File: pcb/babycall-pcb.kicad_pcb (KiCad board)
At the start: 2 copper layers, 1 part, among them U1 ESP32-C3-MINI-1-H4X

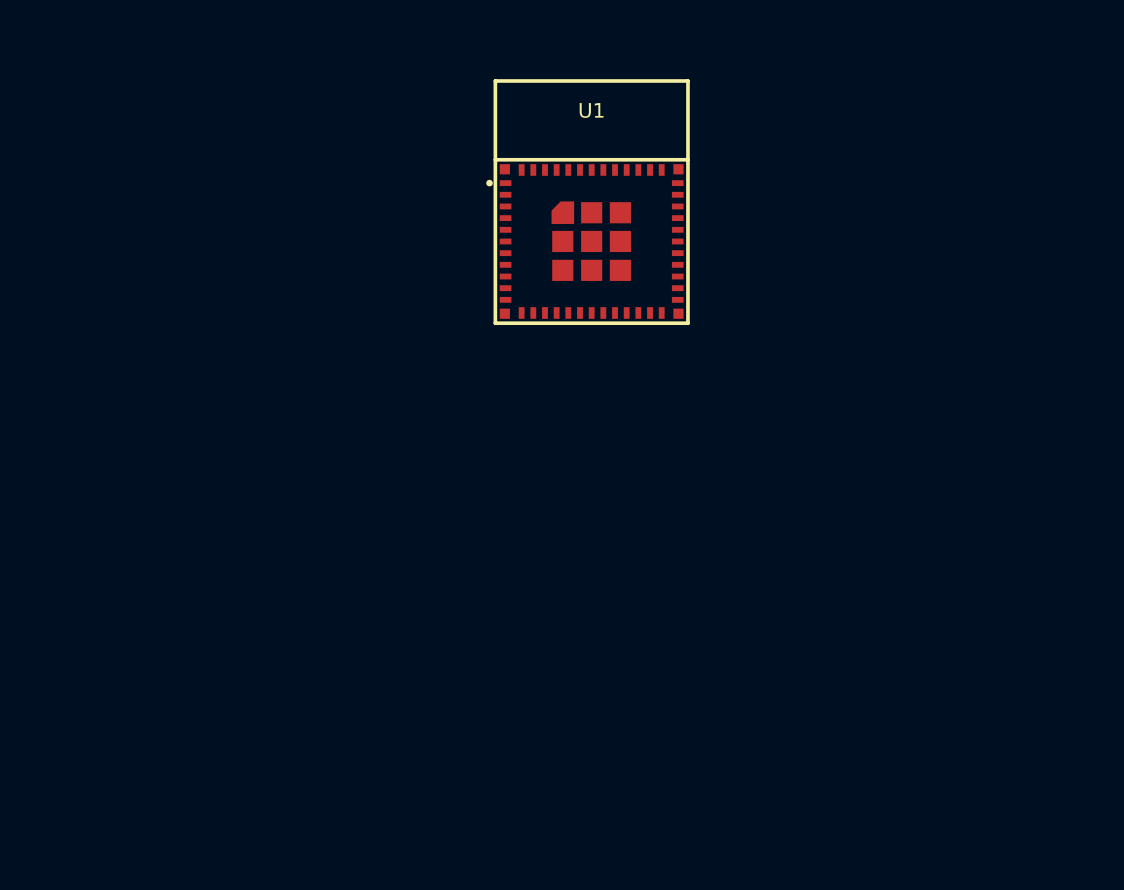
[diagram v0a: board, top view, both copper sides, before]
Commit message: Claude stuff, and gitignore
Also some models for pcb
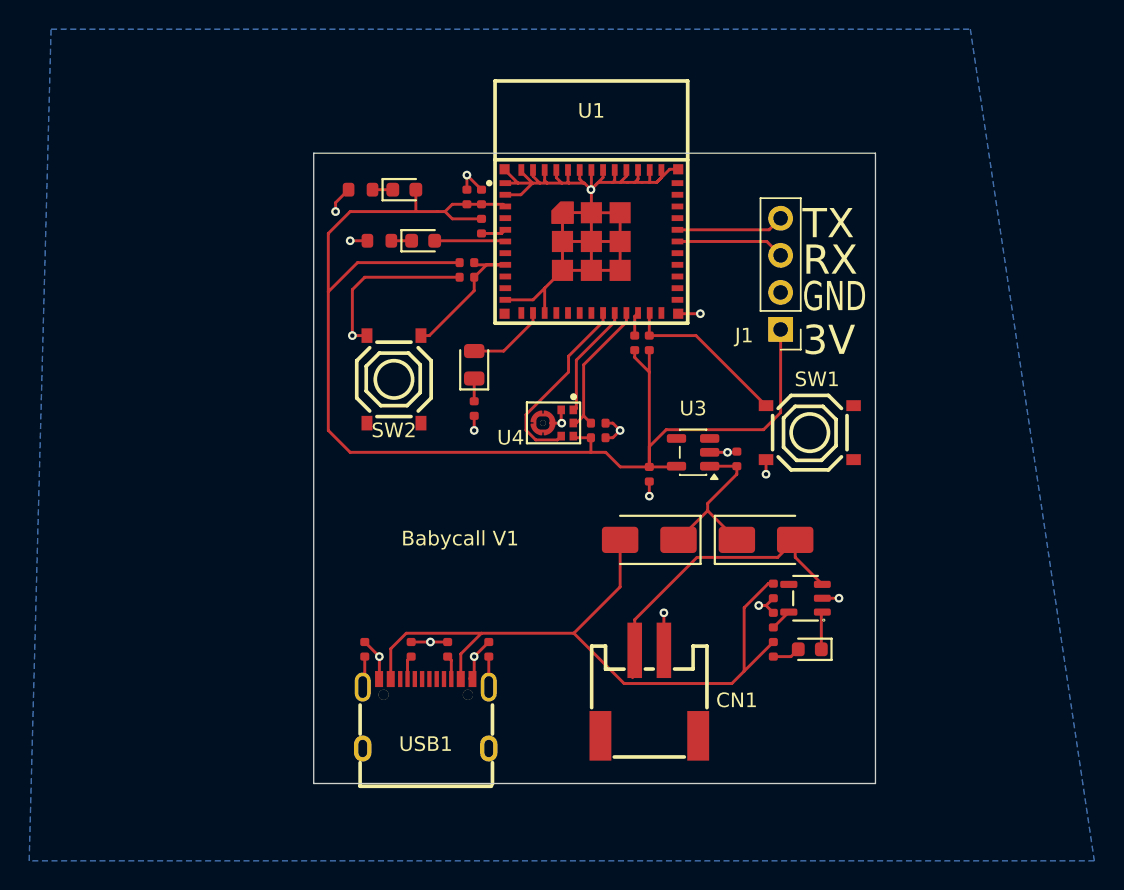
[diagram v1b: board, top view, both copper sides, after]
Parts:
- added C1: 1uF, PCM_JLCPCB:C_0402, F.Cu at (144.5, 90.0)
- added C10: 1uF, PCM_JLCPCB:C_0402, F.Cu at (162.0, 108.0)
- added C11: 1uF, PCM_JLCPCB:C_0402, F.Cu at (156.0, 109.0)
- added C12: 1uF, PCM_JLCPCB:C_0402, F.Cu at (152.5, 106.5)
- added C2: 100nF, PCM_JLCPCB:C_0402, F.Cu at (143.5, 90.0)
- added C3: 1uF, PCM_JLCPCB:C_0402, F.Cu at (143.5, 95.5)
- added C7: 100nF, PCM_JLCPCB:C_0402, F.Cu at (136.5, 121.0)
- added C8: 100nF, PCM_JLCPCB:C_0402, F.Cu at (145.0, 121.0)
- added C9: 1uF, PCM_JLCPCB:C_0402, F.Cu at (164.5, 117.0)
- added CN1: S2B-PH-SM4-TB(LF)(SN), jlcpcb:CONN-SMD_P2.00_S2B-PH-SM4-TB-LF-SN, F.Cu at (156.0, 124.0)
- added D2: Red, PCM_JLCPCB:D_0603, F.Cu at (139.2, 89.5)
- added D3: Green, PCM_JLCPCB:D_0805, F.Cu at (144.0, 101.5)
- added D4: Yellow, PCM_JLCPCB:D_0603, F.Cu at (140.5, 93.0)
- added D5: Red, PCM_JLCPCB:D_0603, F.Cu at (167.0, 121.0)
- added D6: SS34, PCM_JLCPCB:D_SMA, F.Cu at (156.0, 113.5)
- added D7: SS34, PCM_JLCPCB:D_SMA, F.Cu at (164.0, 113.5)
- added J1: Conn_01x04_Pin, Connector_PinHeader_2.54mm:PinHeader_1x04_P2.54mm_Vertical, F.Cu at (165.0, 99.1)
- added R1: 10kΩ, PCM_JLCPCB:R_0402, F.Cu at (143.5, 94.5)
- added R10: 270Ω, PCM_JLCPCB:R_0603, F.Cu at (136.2, 89.5)
- added R11: 220Ω, PCM_JLCPCB:R_0402, F.Cu at (144.0, 104.5)
- added R12: 270Ω, PCM_JLCPCB:R_0603, F.Cu at (137.5, 93.0)
- added R13: 100kΩ, PCM_JLCPCB:R_0402, F.Cu at (152.5, 105.5)
- added R14: 330Ω, PCM_JLCPCB:R_0402, F.Cu at (164.5, 121.0)
- added R2: 4.7kΩ, PCM_JLCPCB:R_0402, F.Cu at (164.5, 119.0)
- added R3: 10kΩ, PCM_JLCPCB:R_0402, F.Cu at (144.5, 92.0)
- added R4: 10kΩ, PCM_JLCPCB:R_0402, F.Cu at (155.0, 100.0)
- added R6: 10kΩ, PCM_JLCPCB:R_0402, F.Cu at (156.0, 100.0)
- added R7: 5.1kΩ, PCM_JLCPCB:R_0402, F.Cu at (142.2, 121.0)
- added R8: 5.1kΩ, PCM_JLCPCB:R_0402, F.Cu at (139.7, 121.0)
- added SW1: TS-1187A-B-A-B, jlcpcb:SW-SMD_4P-L5.1-W5.1-P3.70-LS6.5-TL_H1.5, F.Cu at (167.0, 106.2)
- added SW2: TS-1187A-B-A-B, jlcpcb:SW-SMD_4P-L5.1-W5.1-P3.70-LS6.5-TL_H1.5, F.Cu at (138.5, 102.5)
- added U3: AP2112K-3.3, Package_TO_SOT_SMD:SOT-23-5, F.Cu at (159.0, 107.5)
- added U4: ICS-43434_C5656610, jlcpcb:MIC-SMD_6P-L3.5-W2.7-P0.90-BL, F.Cu at (149.5, 105.5)
- added U5: TP4054, PCM_JLCPCB:SOT-23-5_L3.0-W1.7-P0.95-LS2.8-BL, F.Cu at (166.7, 117.5)
- added USB1: TYPE-C 16PIN 2MD(073), jlcpcb:USB-C-SMD_TYPE-C-6PIN-2MD-073, F.Cu at (140.7, 125.4)
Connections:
- U1 pad 1: unconnected-(U1-GND-Pad1) -> GND
- U1 pad 11: unconnected-(U1-GND-Pad11) -> GND
- U1 pad 13: unconnected-(U1-IO1-Pad13) -> /GLED
- U1 pad 14: unconnected-(U1-GND-Pad14) -> GND
- U1 pad 19: unconnected-(U1-IO5-Pad19) -> /MEMS_SCK
- U1 pad 2: unconnected-(U1-GND-Pad2) -> GND
- U1 pad 20: unconnected-(U1-IO6-Pad20) -> /MEMS_WS
- U1 pad 21: unconnected-(U1-IO7-Pad21) -> /MEMS_SD
- U1 pad 22: unconnected-(U1-IO8-Pad22) -> Net-(U1-IO8)
- U1 pad 23: unconnected-(U1-IO9-Pad23) -> /BOOT
- U1 pad 3: unconnected-(U1-3V3-Pad3) -> +3V3
- U1 pad 30: unconnected-(U1-RXD0-Pad30) -> Net-(J1-Pin_3)
- U1 pad 31: unconnected-(U1-TXD0-Pad31) -> Net-(J1-Pin_4)
- U1 pad 36: unconnected-(U1-GND-Pad36) -> GND
- U1 pad 37: unconnected-(U1-GND-Pad37) -> GND
- U1 pad 38: unconnected-(U1-GND-Pad38) -> GND
- U1 pad 39: unconnected-(U1-GND-Pad39) -> GND
- U1 pad 40: unconnected-(U1-GND-Pad40) -> GND
- U1 pad 41: unconnected-(U1-GND-Pad41) -> GND
- U1 pad 42: unconnected-(U1-GND-Pad42) -> GND
- U1 pad 43: unconnected-(U1-GND-Pad43) -> GND
- U1 pad 44: unconnected-(U1-GND-Pad44) -> GND
- U1 pad 45: unconnected-(U1-GND-Pad45) -> GND
- U1 pad 46: unconnected-(U1-GND-Pad46) -> GND
- U1 pad 47: unconnected-(U1-GND-Pad47) -> GND
- U1 pad 48: unconnected-(U1-GND-Pad48) -> GND
- U1 pad 49: unconnected-(U1-GND-Pad49) -> GND
- U1 pad 5: unconnected-(U1-IO2-Pad5) -> Net-(U1-IO2)
- U1 pad 50: unconnected-(U1-GND-Pad50) -> GND
- U1 pad 51: unconnected-(U1-GND-Pad51) -> GND
- U1 pad 52: unconnected-(U1-GND-Pad52) -> GND
- U1 pad 53: unconnected-(U1-GND-Pad53) -> GND
- U1 pad 6: unconnected-(U1-IO3-Pad6) -> /YLED
- U1 pad 8: unconnected-(U1-EN-Pad8) -> /RESET
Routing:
- net GND: track 0.00 -> 108.0 mm, vias 0 -> 18
- net +3V3: track 0.00 -> 94.7 mm
- net +5V: track 0.00 -> 49.8 mm
- net +BATT: track 0.00 -> 19.2 mm
- net /MEMS_SCK: track 0.00 -> 13.0 mm
- net /BOOT: track 0.00 -> 11.6 mm
- net /USB+BATT: track 0.00 -> 11.5 mm
- net /RESET: track 0.00 -> 10.5 mm
- net /MEMS_SD: track 0.00 -> 9.88 mm
- net /MEMS_WS: track 0.00 -> 7.89 mm
- net Net-(J1-Pin_3): track 0.00 -> 7.46 mm
- net Net-(J1-Pin_4): track 0.00 -> 7.40 mm
- net /GLED: track 0.00 -> 5.50 mm
- net /YLED: track 0.00 -> 4.86 mm
- net Net-(U5-CHRG): track 0.00 -> 2.58 mm
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- added copper zone on B.Cu, net GND
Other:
- board outline added: 38.5 x 43.2 mm
- board text added: "3V"
- board text added: "Babycall V1"
- board text added: "GND"
- board text added: "RX"
- board text added: "TX"
